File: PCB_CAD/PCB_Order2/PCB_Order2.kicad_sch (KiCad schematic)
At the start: 48 parts

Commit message: more pcb design things. RAM and Flash wiring
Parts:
- LLS In1: renamed from LLS In
- LLS Out1: renamed from LLS Out
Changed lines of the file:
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@@
 		(dnp no)
 		(fields_autoplaced yes)
-		(property "Reference" "LLS Out"
+		(property "Reference" "LLS Out1"
 			(at 687.07 185.42 0)
 			(effects
@@
 			(project ""
 				(path "/85a2a93a-53e0-46c8-b7f5-ee661b6f3053"
-					(reference "LLS Out")
+					(reference "LLS Out1")
 					(unit 1)
 				)
@@
 		(dnp no)
 		(fields_autoplaced yes)
-		(property "Reference" "LLS In"
+		(property "Reference" "LLS In1"
 			(at 280.67 250.19 0)
 			(effects
@@
 			(project ""
 				(path "/85a2a93a-53e0-46c8-b7f5-ee661b6f3053"
-					(reference "LLS In")
+					(reference "LLS In1")
 					(unit 1)
 				)

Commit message: pcb layout stuff
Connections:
- net FMC_11 is gone; now on net FMC_A11: RAM1.35 (A11)
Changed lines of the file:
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@@
 		)
 	)
-	(label "FMC_11"
+	(label "FMC_A11"
 		(at 556.26 344.17 0)
 		(fields_autoplaced yes)

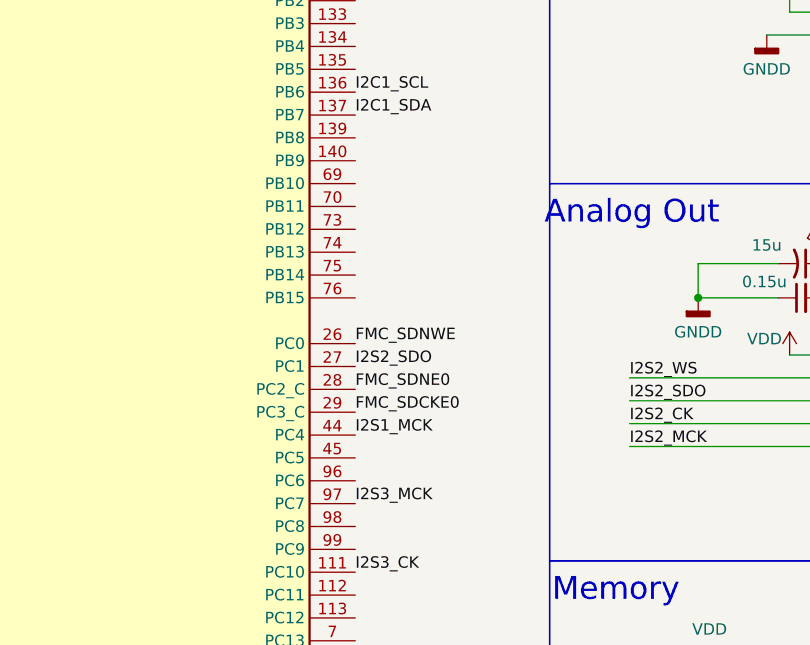
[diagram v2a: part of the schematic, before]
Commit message: added i2s2 pins on kicad schematic
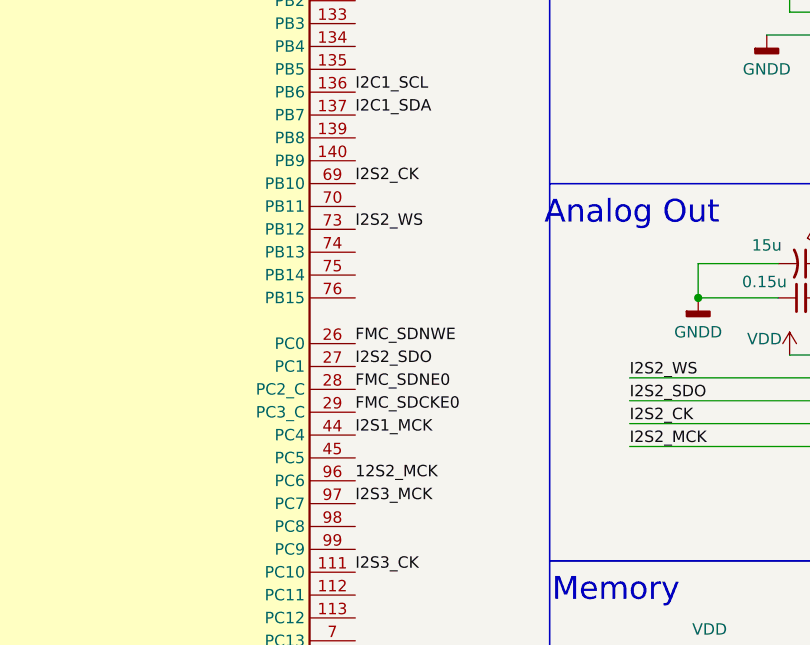
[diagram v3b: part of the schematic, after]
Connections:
- net I2S2_CK: now also uController1.69 (PB10)
- net I2S2_WS: now also uController1.73 (PB12)
- net 12S2_MCK: now reaches uController1.96 (PC6)
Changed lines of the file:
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@@
+		)
+	)
+	(label "I2S2_WS"
+		(at 462.28 246.38 0)
+		(fields_autoplaced yes)
+		(effects
+			(font
+				(size 1.27 1.27)
+			)
+			(justify left bottom)
 		)
 	)
@@
 		)
 	)
+	(label "12S2_MCK"
+		(at 462.28 274.32 0)
+		(fields_autoplaced yes)
+		(effects
+			(font
+				(size 1.27 1.27)
+			)
+			(justify left bottom)
+		)
+	)
 	(label "FMC_D12"
 		(at 556.26 311.15 0)
@@
 		(fields_autoplaced yes)
 		(effects
+			(font
+				(size 1.27 1.27)
+			)
+			(justify left bottom)
+		)
+	)
+	(label "I2S2_CK"
+		(at 462.28 241.3 0)
+		(fields_autoplaced yes)
+		(effects

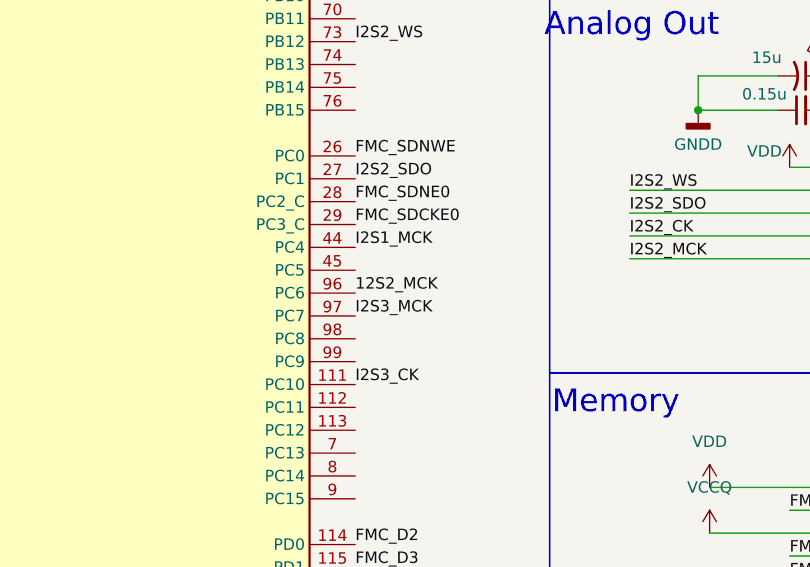
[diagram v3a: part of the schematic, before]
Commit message: corrected 1 small i2s2 error
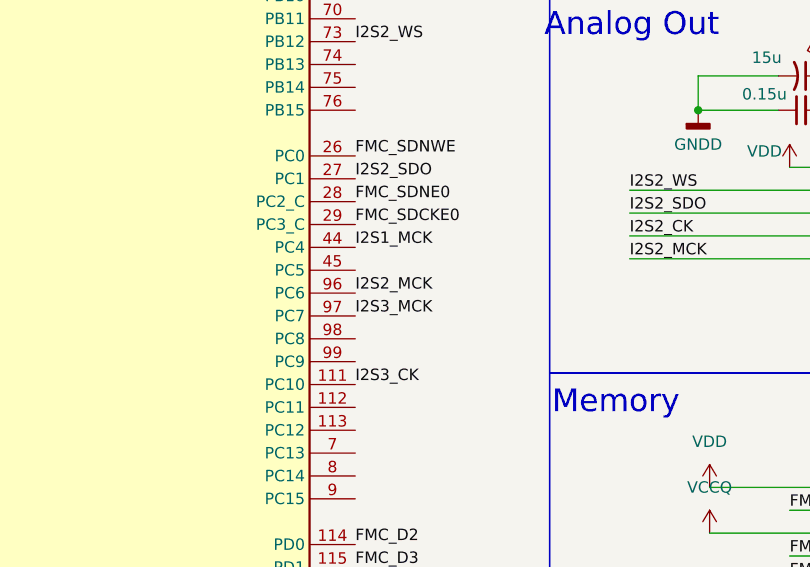
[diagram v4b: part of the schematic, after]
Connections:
- net 12S2_MCK is gone; now on net I2S2_MCK: uController1.96 (PC6)
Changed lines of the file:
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@@
 		)
 	)
-	(label "12S2_MCK"
+	(label "I2S2_MCK"
 		(at 462.28 274.32 0)
 		(fields_autoplaced yes)

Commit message: pcb'd dix9211 and lss with power
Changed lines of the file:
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@@
 	(paper "User" 3048 2794)
 	(junction
-		(at 523.24 219.71)
-		(diameter 0)
-		(color 0 0 0 0)
-	)
-	(junction
 		(at 514.35 250.19)
 		(diameter 0)
@@
 	)
 	(junction
+		(at 520.7 219.71)
+		(diameter 0)
+		(color 0 0 0 0)
+	)
+	(junction
 		(at 308.61 185.42)
 		(diameter 0)
@@
 	)
 	(junction
-		(at 518.16 219.71)
-		(diameter 0)
-		(color 0 0 0 0)
-	)
-	(junction
 		(at 300.99 254)
 		(diameter 0)
@@
 	(wire
 		(pts
-			(xy 523.24 219.71) (xy 535.94 219.71)
-		)
-		(stroke
-			(width 0)
-			(type default)
-		)
-	)
-	(wire
-		(pts
 			(xy 237.49 278.13) (xy 256.54 278.13)
 		)
@@
 	(wire
 		(pts
-			(xy 518.16 219.71) (xy 523.24 219.71)
+			(xy 518.16 219.71) (xy 520.7 219.71)
 		)
 		(stroke
@@
 	(wire
 		(pts
-			(xy 642.62 173.99) (xy 642.62 176.53)
+			(xy 520.7 219.71) (xy 523.24 219.71)
 		)
 		(stroke
@@
 	(wire
 		(pts
-			(xy 533.4 257.81) (xy 546.1 257.81)
+			(xy 642.62 173.99) (xy 642.62 176.53)
 		)
 		(stroke
@@
 	(wire
 		(pts
-			(xy 510.54 321.31) (xy 523.24 321.31)
+			(xy 533.4 257.81) (xy 546.1 257.81)
 		)
 		(stroke
@@
 	(wire
 		(pts
-			(xy 222.25 266.7) (xy 231.14 266.7)
+			(xy 510.54 321.31) (xy 523.24 321.31)
 		)
 		(stroke
@@
 	(wire
 		(pts
-			(xy 596.9 260.35) (xy 605.79 260.35)
+			(xy 222.25 266.7) (xy 231.14 266.7)
 		)
 		(stroke
@@
 	(wire
 		(pts
-			(xy 514.35 219.71) (xy 518.16 219.71)
+			(xy 596.9 260.35) (xy 605.79 260.35)
 		)
 		(stroke
@@
 	(symbol
 		(lib_id "power:GNDD")
-		(at 514.35 219.71 0)
+		(at 520.7 219.71 0)
 		(unit 1)
 		(exclude_from_sim no)
@@
 		(dnp no)
 		(property "Reference" "#PWR043"
-			(at 514.35 226.06 0)
+			(at 520.7 226.06 0)
 			(effects
 				(font
@@
 		)
 		(property "Value" "GNDD"
-			(at 519.43 221.234 0)
+			(at 516.636 220.98 0)
 			(effects
 				(font
@@
 		)
 		(property "Footprint" ""
-			(at 514.35 219.71 0)
+			(at 520.7 219.71 0)
 			(effects
 				(font
@@
 		)
 		(property "Datasheet" ""
-			(at 514.35 219.71 0)
+			(at 520.7 219.71 0)
 			(effects
 				(font
@@
 		)
 		(property "Description" "Power symbol creates a global label with name \"GNDD\" , digital ground"
-			(at 514.35 219.71 0)
+			(at 520.7 219.71 0)
 			(effects
 				(font
@@
 					(unit 1)
 				)
+			)
+		)
+	)
+	(symbol
+		(lib_id "power:GNDD")
+		(at 535.94 219.71 0)
+		(mirror y)
+		(unit 1)
+		(exclude_from_sim no)
+		(in_bom yes)
+		(on_board yes)
+		(dnp no)
+		(property "Reference" "#PWR070"
+			(at 535.94 226.06 0)
+			(effects
+				(font
+					(size 1.27 1.27)
+				)
+				(hide yes)
+			)
+		)
+		(property "Value" "GNDD"
+			(at 530.86 221.234 0)
+			(effects
+				(font
+					(size 1.27 1.27)
+				)
+			)
+		)
+		(property "Footprint" ""
+			(at 535.94 219.71 0)
+			(effects
+				(font
+					(size 1.27 1.27)
+				)
+				(hide yes)
+			)
+		)
+		(property "Datasheet" ""
+			(at 535.94 219.71 0)
+			(effects
+				(font
+					(size 1.27 1.27)
+				)
+				(hide yes)
+			)
+		)
+		(property "Description" "Power symbol creates a global label with name \"GNDD\" , digital ground"
+			(at 535.94 219.71 0)
+			(effects
+				(font
+					(size 1.27 1.27)
+				)
+				(hide yes)
+			)
+		)
+		(pin "1"
+		)
+		(instances
+			(project "PCB_Order2"
+				(path "/85a2a93a-53e0-46c8-b7f5-ee661b6f3053"
+					(reference "#PWR070")
+					(unit 1)
+				)

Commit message: current schematic work from Isaac's side
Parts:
- added K1: ~, symbol custom:86jb2
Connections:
- net KP_Col5: now reaches uController1.1 (PE2)
- net KP_Col5: now also K1.1 (F)
- net KP_Col4: now reaches uController1.2 (PE3)
- net KP_Col4: now also K1.2 (G)
- net KP_Row1: now reaches uController1.3 (PE4)
- net KP_Row1: now also K1.4 (J)
- net KP_Col3: now reaches uController1.4 (PE5)
- net KP_Col3: now also K1.5 (K)
- net KP_Row2: now reaches uController1.5 (PE6)
- net KP_Row2: now also K1.6 (L)
- net KP_Row3: now reaches uController1.7 (PC13)
- net KP_Row3: now also K1.7 (M)
- net KP_Col2: now reaches uController1.8 (PC14)
- net KP_Col2: now also K1.8 (N)
- net KP_Col1: now reaches uController1.9 (PC15)
- net KP_Col1: now also K1.9 (P)
- no-connect marks 0 -> 1

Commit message: dac power and digital out done
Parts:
- removed DacMute_CurrentLimit1: 10k, Resistor_SMD:R_0603_1608Metric_Pad0.98x0.95mm_HandSolder, symbol Device:R_Small_US
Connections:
- net SPDIFRX_IN0: now also uController1.123 (PD7)
- net VDD: now also DAC1.4 (MUTEB)
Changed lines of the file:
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@@
 	(wire
 		(pts
-			(xy 510.54 260.35) (xy 523.24 260.35)
+			(xy 510.54 260.35) (xy 546.1 260.35)
 		)
 		(stroke
@@
 	(wire
 		(pts
-			(xy 528.32 260.35) (xy 546.1 260.35)
-		)
-		(stroke
-			(width 0)
-			(type default)
-		)
-	)
-	(wire
-		(pts
 			(xy 386.08 287.02) (xy 398.78 287.02)
 		)
@@
 		)
 	)
+	(label "SPDIFRX_IN0"
+		(at 462.28 320.04 0)
+		(fields_autoplaced yes)
+		(effects
+			(font
+				(size 1.27 1.27)
+			)
+			(justify left bottom)
+		)
+	)
 	(label "FMC_A4"
 		(at 556.26 359.41 0)
@@
 					(unit 1)
 				)
-			)
-		)
-	)
-	(symbol
-		(lib_id "Device:R_Small_US")
-		(at 525.78 260.35 90)
-		(unit 1)
-		(exclude_from_sim no)
-		(in_bom yes)
-		(on_board yes)
-		(dnp no)
-		(property "Reference" "DacMute_CurrentLimit1"
-			(at 525.78 254 90)
-			(effects
-				(font
-					(size 1.27 1.27)
-				)
-				(hide yes)
-			)
-		)
-		(property "Value" "10k"
-			(at 529.336 261.62 90)
-			(effects
-				(font
-					(size 1.27 1.27)
-				)
-			)
-		)
-		(property "Footprint" "Resistor_SMD:R_0603_1608Metric_Pad0.98x0.95mm_HandSolder"
-			(at 525.78 260.35 0)
-			(effects
-				(font
-					(size 1.27 1.27)
-				)
-				(hide yes)
-			)
-		)
-		(property "Datasheet" "~"
-			(at 525.78 260.35 0)
-			(effects
-				(font
-					(size 1.27 1.27)
-				)
-				(hide yes)
-			)
-		)
-		(property "Description" "Resistor, small US symbol"
-			(at 525.78 260.35 0)
-			(effects
-				(font
-					(size 1.27 1.27)
-				)
-				(hide yes)
-			)
-		)
-		(pin "2"
-		)
-		(pin "1"
-		)
-		(instances
-			(project ""
-				(path "/85a2a93a-53e0-46c8-b7f5-ee661b6f3053"
-					(reference "DacMute_CurrentLimit1")
-					(unit 1)
-				)

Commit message: schematic fix adc, voltage divider, keypad, update cubeMX with kp pins
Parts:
- removed C2, C3, C4, C6: 10uF, Capacitor_SMD:C_0805_2012Metric_Pad1.18x1.45mm_HandSolder, symbol Device:C_Polarized_Small
- removed C5, C7: 0.1uF, Capacitor_SMD:C_0805_2012Metric_Pad1.18x1.45mm_HandSolder, symbol Device:C_Small
- removed C8: 1uF, Capacitor_SMD:C_0805_2012Metric_Pad1.18x1.45mm_HandSolder, symbol Device:C_Polarized_Small
- added adcBead: 600, symbol Device:FerriteBead_Small
- added adcReset_rc_cap: 47u, symbol Device:C_Polarized_Small_US
- added adcReset_rc_res: 100k, symbol Device:R_Small_US
- added adc_L_acCouple, adc_R_acCouple: 10u, symbol Device:C_Polarized_Small_US
- added adc_aSupply_bulk, adc_dSupply_bulk1: 15u, symbol Device:C_Polarized_Small_US
- added adc_aSupply_noise, adc_dSupply_noise1: 0.15u, symbol Device:C_Small
- added adc_rego: 1u, symbol Device:C_Polarized_Small_US
- Dac_ChargePump_bead1: value *TBD* -> 600
- K1: footprint (none) -> Connector_PinSocket_2.54mm:PinSocket_1x09_P2.54mm_Vertical
- VdivHigh: renamed from R2; value 6.2k -> 8.87k
- VdivLow: renamed from R3; value 1.6k -> 2.21k
- adc_vcom: renamed from C1; value 0.47uF -> 0.47u
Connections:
- net GNDD: now also adcReset_rc_cap.2, adc_aSupply_bulk.2, adc_aSupply_noise.1, adc_dSupply_bulk1.2, adc_dSupply_noise1.2, adc_rego.2
- net VDD: now also adcBead.1, adcReset_rc_cap.1, adcReset_rc_res.2, adc_dSupply_bulk1.1, adc_dSupply_noise1.1
- net VDDA: no longer ADC1.5 (VA)
- net at AnalogIn1.2: now also adc_R_acCouple.1
- net at ADC1.2 (RIN): now also adc_R_acCouple.2
- net KP_Row4: now reaches K1.3 (H)
- net KP_Row4: now also uController1.19 (PF7)
- net at ADC1.8 (REGO): now also adc_rego.1
- net at AnalogIn1.3: now also adc_L_acCouple.1
- net at ADC1.3 (LIN): now also adc_L_acCouple.2
- net ADC_Reset: no longer names the net of ADC1.13 (~{PDN})
- net ADC_Reset: now also adcReset_rc_res.1
- new net: ADC1.5 (VA), adcBead.2, adc_aSupply_bulk.1, adc_aSupply_noise.2
- no-connect marks 1 -> 0
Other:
- moved on the sheet: AnalogIn1
